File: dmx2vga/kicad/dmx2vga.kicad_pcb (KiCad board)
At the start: 2 copper layers, 30 x 55 mm, 13 parts, among them J1 DMX In, J2 DMX Thru, J3 Programming Pins, SW1 RotaryEncoder_Switch, SW2 SW_Push, U1 Olimex_MOD-WIFI-ESP8266-DEV, U2 MAX485E

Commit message: fix positioning
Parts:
- added REF**: MountingHole_3.2mm_M3_DIN965_Pad, MountingHole:MountingHole_3.2mm_M3_DIN965_Pad, F.Cu at (60.0, 95.0)
- added REF**: MountingHole_3.2mm_M3_DIN965_Pad, MountingHole:MountingHole_3.2mm_M3_DIN965_Pad, F.Cu at (60.0, 35.0)
- added REF**: MountingHole_3.2mm_M3_DIN965_Pad, MountingHole:MountingHole_3.2mm_M3_DIN965_Pad, F.Cu at (175.0, 95.0)
- added REF**: MountingHole_3.2mm_M3_DIN965_Pad, MountingHole:MountingHole_3.2mm_M3_DIN965_Pad, F.Cu at (175.0, 35.0)
- moved SW2 129.2 mm to (141.2, 75.8), turned to 90 degrees
- moved SW1 122.4 mm to (152.5, 87.4), turned to 180 degrees
- moved Brd1 121.5 mm to (135.7, 46.6)
- moved U1 106.6 mm to (108.0, 74.9)
- moved J3 78.1 mm to (104.9, 38.0), turned to 90 degrees
- moved J1 62.3 mm to (76.2, 49.7)
- moved U2 46.3 mm to (98.0, 46.9)
- moved R4 33.2 mm to (126.0, 70.0)
- moved R2 29.1 mm to (126.0, 72.5)
- moved R3 28.6 mm to (126.0, 77.5)
- moved R1 27.8 mm to (126.0, 75.0)
- moved J2 25.1 mm to (83.6, 78.8)
- moved JP1 9.73 mm to (96.0, 40.2), turned to 180 degrees
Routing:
- net GPIO-5: track 0.00 -> 131.2 mm
- net DMX3: track 0.00 -> 56.9 mm
- net DMX2: track 0.00 -> 54.0 mm
- net RESET: track 0.00 -> 53.9 mm
- net RX: track 0.00 -> 53.3 mm, vias 0 -> 1
- net Net-(JP1-B): track 0.00 -> 46.9 mm
- net GND: track 0.00 -> 46.6 mm
- net GPIO-15: track 0.00 -> 37.5 mm
- net GPIO-13: track 0.00 -> 37.2 mm
- net GPIO-12: track 0.00 -> 37.2 mm
- net TX: track 0.00 -> 36.6 mm, vias 0 -> 1
- net GPIO-4: track 0.00 -> 34.6 mm
- net +5V: track 0.00 -> 30.9 mm, vias 0 -> 4
- net GPIO-2: track 0.00 -> 30.7 mm
- net GPIO-0: track 0.00 -> 29.6 mm
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- added copper zone on F.Cu, net +5V
- added copper zone on B.Cu, net GND
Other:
- board size 30 x 55 mm -> 125 x 70 mm

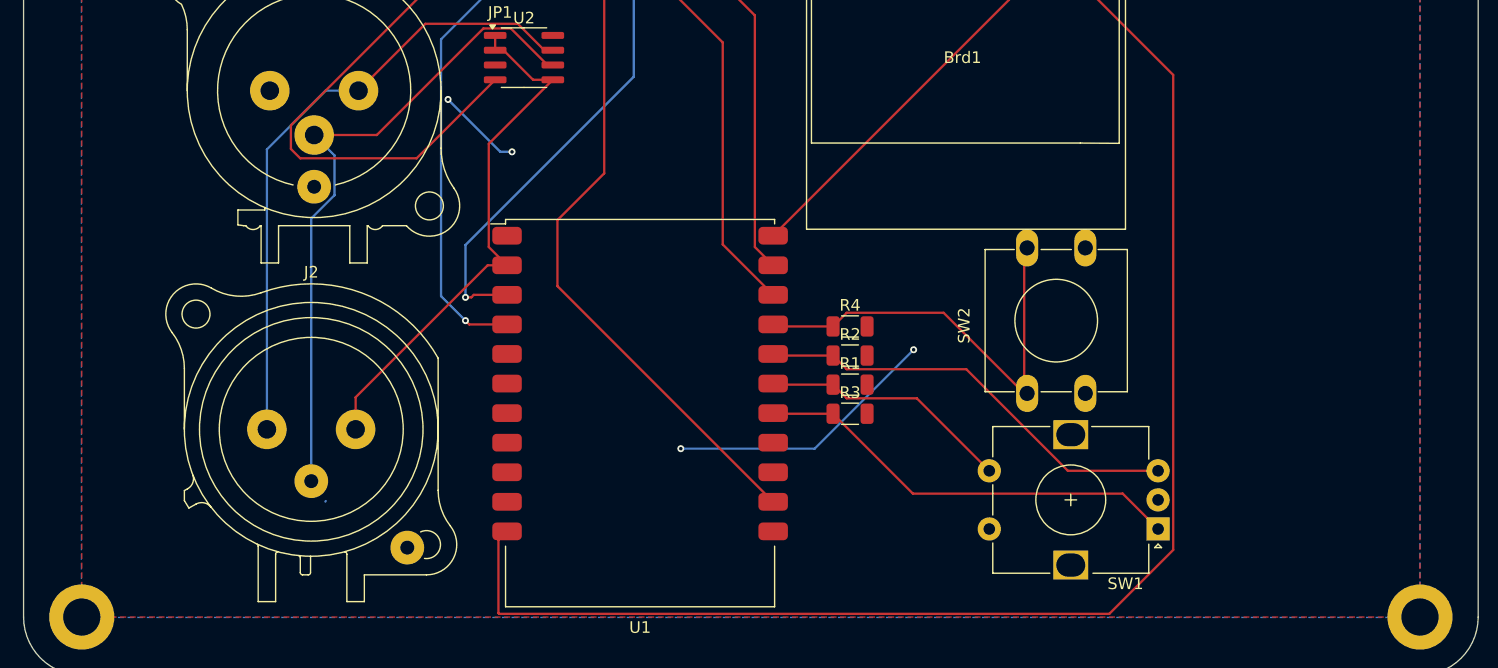
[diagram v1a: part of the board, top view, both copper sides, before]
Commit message: feat(kicad): add icon; add vga connector
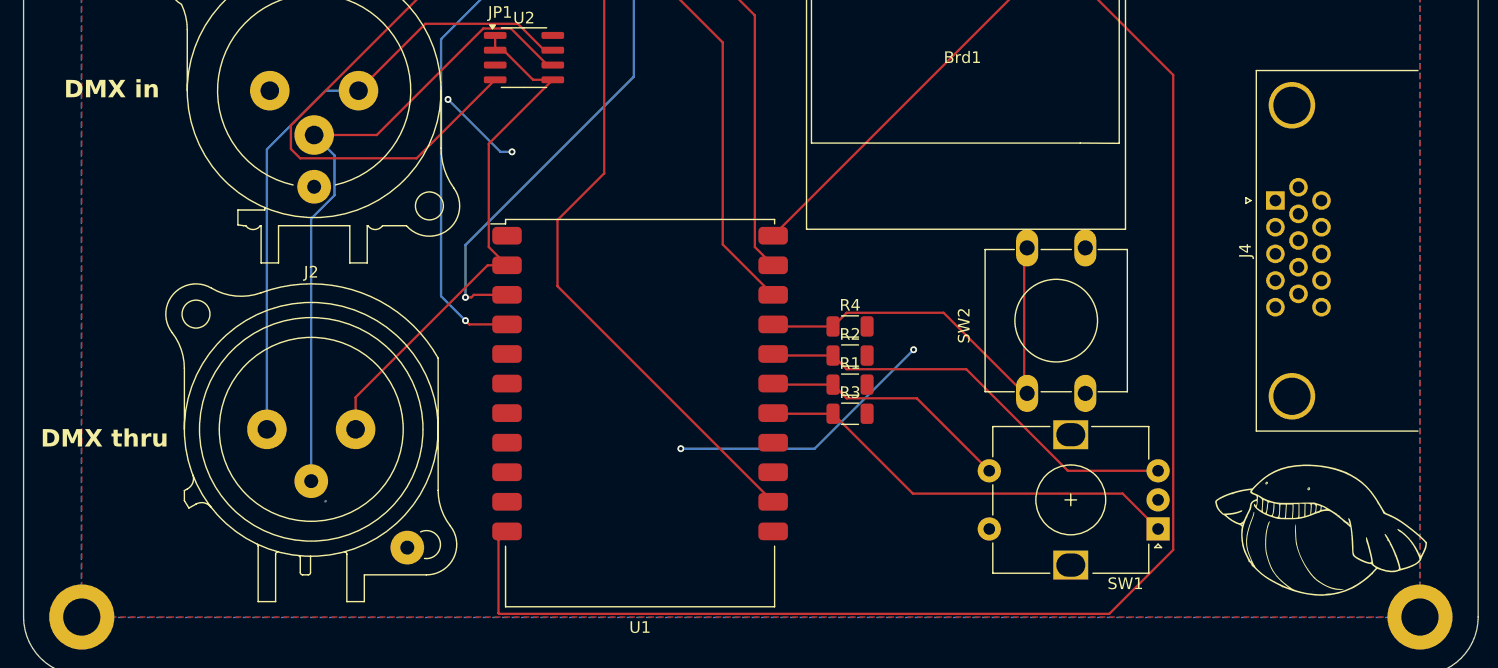
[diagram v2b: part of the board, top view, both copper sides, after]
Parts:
- added G***: LOGO, library:wailmer_small, F.Cu at (166.5, 87.5)
- added G***: LOGO, library:wailmer, B.Cu at (115.0, 67.5)
- added J4: DE15_Receptacle_HighDensity, Connector_Dsub:DSUB-15-HD_Female_Horizontal_P2.29x1.98mm_EdgePinOffset8.35mm_Housed_MountingHolesOffset10.89mm, F.Cu at (162.6, 59.2)
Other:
- board text added: "DMX in"
- board text added: "DMX thru"
